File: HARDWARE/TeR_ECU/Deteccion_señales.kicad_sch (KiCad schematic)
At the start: 4 parts

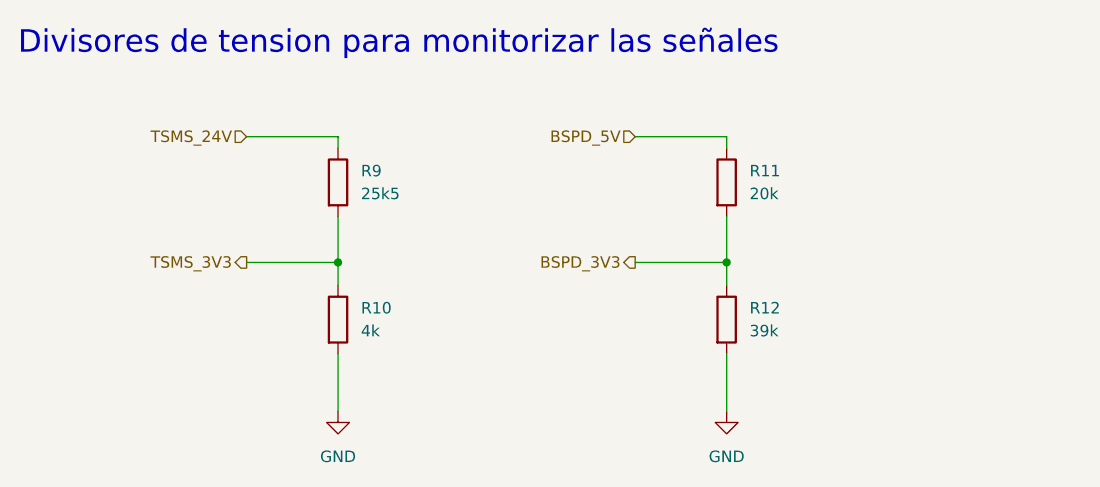
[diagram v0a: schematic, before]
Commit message: Rethought layout and footprints and fixed fuse normative problem
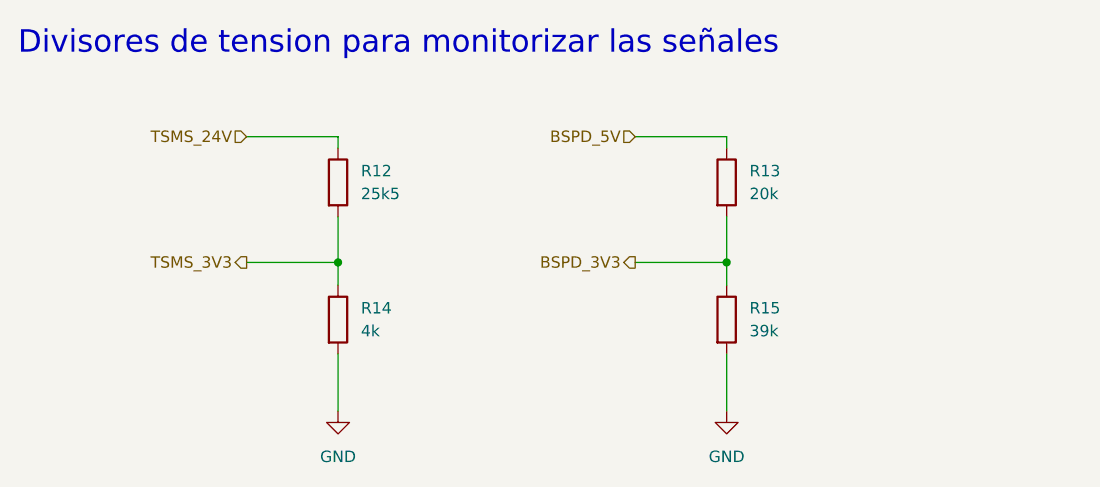
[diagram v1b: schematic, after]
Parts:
- renumbered R9 to R12, R11 to R13, R10 to R14, R12 to R15
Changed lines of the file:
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@@
   (symbol (lib_id "Device:R") (at 121.92 72.39 0) (unit 1)
     (in_bom yes) (on_board yes) (dnp no) (fields_autoplaced)
-    (property "Reference" "R9" (at 124.46 71.12 0)
+    (property "Reference" "R12" (at 124.46 71.12 0)
       (effects (font (size 1.27 1.27)) (justify left))
     )
@@
       (project "TeR_ECU"
         (path "/84413845-c4f3-4743-bcd2-a67649c90902/a7e5ef7e-c831-4d4f-a194-90a98bc5e16b"
-          (reference "R9") (unit 1)
+          (reference "R12") (unit 1)
         )
       )
@@
   (symbol (lib_id "Device:R") (at 165.1 87.63 0) (unit 1)
     (in_bom yes) (on_board yes) (dnp no) (fields_autoplaced)
-    (property "Reference" "R12" (at 167.64 86.36 0)
+    (property "Reference" "R15" (at 167.64 86.36 0)
       (effects (font (size 1.27 1.27)) (justify left))
     )
@@
       (project "TeR_ECU"
         (path "/84413845-c4f3-4743-bcd2-a67649c90902/a7e5ef7e-c831-4d4f-a194-90a98bc5e16b"
-          (reference "R12") (unit 1)
+          (reference "R15") (unit 1)
         )
       )
@@
   (symbol (lib_id "power:GND") (at 165.1 97.79 0) (unit 1)
     (in_bom yes) (on_board yes) (dnp no) (fields_autoplaced)
-    (property "Reference" "#PWR046" (at 165.1 104.14 0)
+    (property "Reference" "#PWR054" (at 165.1 104.14 0)
       (effects (font (size 1.27 1.27)) hide)
     )
@@
       (project "TeR_ECU"
         (path "/84413845-c4f3-4743-bcd2-a67649c90902/a7e5ef7e-c831-4d4f-a194-90a98bc5e16b"
-          (reference "#PWR046") (unit 1)
+          (reference "#PWR054") (unit 1)
         )
       )
@@
   (symbol (lib_id "power:GND") (at 121.92 97.79 0) (unit 1)
     (in_bom yes) (on_board yes) (dnp no) (fields_autoplaced)
-    (property "Reference" "#PWR044" (at 121.92 104.14 0)
+    (property "Reference" "#PWR053" (at 121.92 104.14 0)
       (effects (font (size 1.27 1.27)) hide)
     )
@@
       (project "TeR_ECU"
         (path "/84413845-c4f3-4743-bcd2-a67649c90902/a7e5ef7e-c831-4d4f-a194-90a98bc5e16b"
-          (reference "#PWR044") (unit 1)
+          (reference "#PWR053") (unit 1)
         )
       )
@@
   (symbol (lib_id "Device:R") (at 165.1 72.39 0) (unit 1)
     (in_bom yes) (on_board yes) (dnp no) (fields_autoplaced)
-    (property "Reference" "R11" (at 167.64 71.12 0)
+    (property "Reference" "R13" (at 167.64 71.12 0)
       (effects (font (size 1.27 1.27)) (justify left))
     )
@@
       (project "TeR_ECU"
         (path "/84413845-c4f3-4743-bcd2-a67649c90902/a7e5ef7e-c831-4d4f-a194-90a98bc5e16b"
-          (reference "R11") (unit 1)
+          (reference "R13") (unit 1)
         )
       )
@@
   (symbol (lib_id "Device:R") (at 121.92 87.63 0) (unit 1)
     (in_bom yes) (on_board yes) (dnp no) (fields_autoplaced)
-    (property "Reference" "R10" (at 124.46 86.36 0)
+    (property "Reference" "R14" (at 124.46 86.36 0)
       (effects (font (size 1.27 1.27)) (justify left))
     )
@@
       (project "TeR_ECU"
         (path "/84413845-c4f3-4743-bcd2-a67649c90902/a7e5ef7e-c831-4d4f-a194-90a98bc5e16b"
-          (reference "R10") (unit 1)
+          (reference "R14") (unit 1)
         )
       )

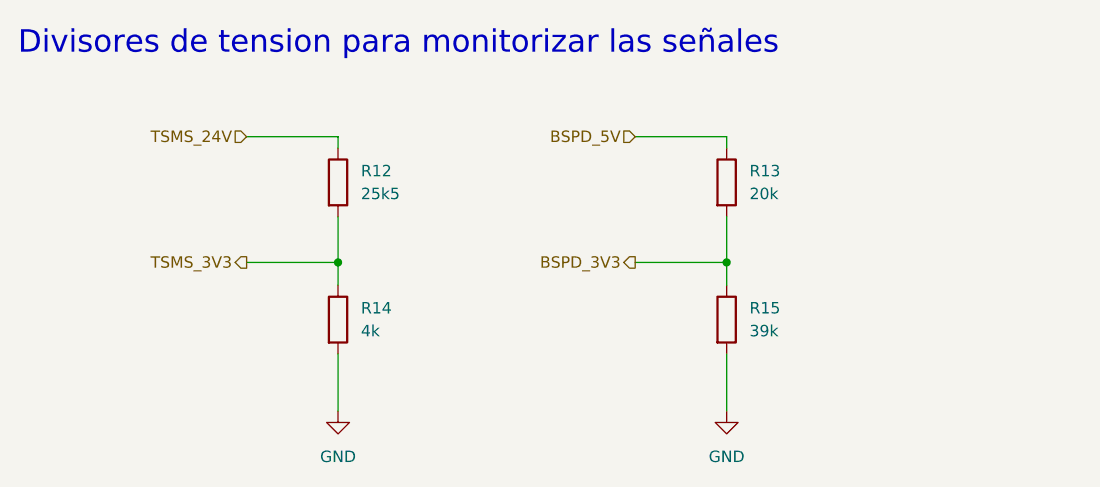
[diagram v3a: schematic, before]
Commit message: Advanced design and added IMU/GPS moduleç
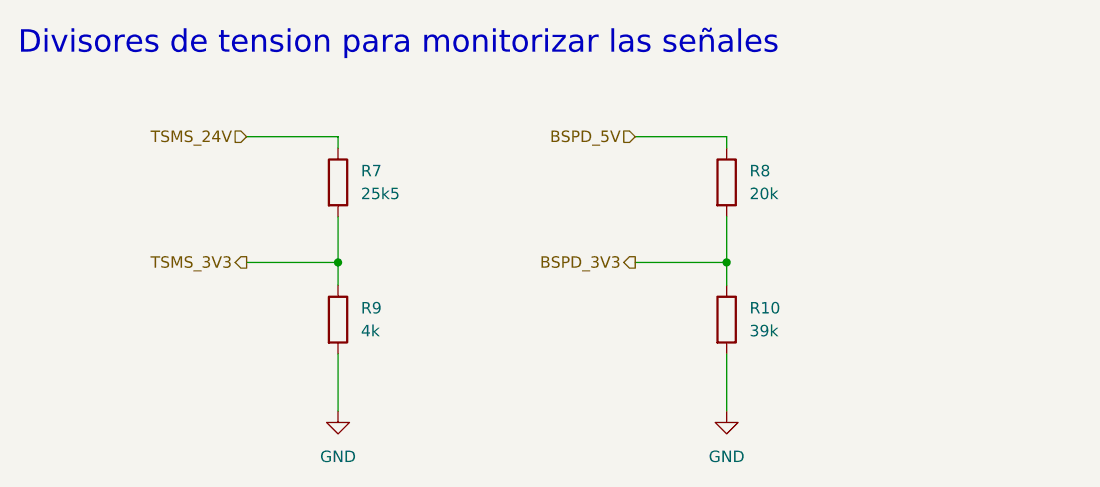
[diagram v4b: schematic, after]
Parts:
- renumbered R15 to R10, R12 to R7, R13 to R8, R14 to R9
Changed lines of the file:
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@@
 		(dnp no)
 		(fields_autoplaced yes)
-		(property "Reference" "R12"
+		(property "Reference" "R7"
 			(at 124.46 71.12 0)
 			(effects
@@
 			(project "TeR_ECU"
 				(path "/84413845-c4f3-4743-bcd2-a67649c90902/a7e5ef7e-c831-4d4f-a194-90a98bc5e16b"
-					(reference "R12")
+					(reference "R7")
 					(unit 1)
 				)
@@
 		(dnp no)
 		(fields_autoplaced yes)
-		(property "Reference" "R15"
+		(property "Reference" "R10"
 			(at 167.64 86.36 0)
 			(effects
@@
 			(project "TeR_ECU"
 				(path "/84413845-c4f3-4743-bcd2-a67649c90902/a7e5ef7e-c831-4d4f-a194-90a98bc5e16b"
-					(reference "R15")
+					(reference "R10")
 					(unit 1)
 				)
@@
 		(dnp no)
 		(fields_autoplaced yes)
-		(property "Reference" "#PWR054"
+		(property "Reference" "#PWR039"
 			(at 165.1 104.14 0)
 			(effects
@@
 			(project "TeR_ECU"
 				(path "/84413845-c4f3-4743-bcd2-a67649c90902/a7e5ef7e-c831-4d4f-a194-90a98bc5e16b"
-					(reference "#PWR054")
+					(reference "#PWR039")
 					(unit 1)
 				)
@@
 		(dnp no)
 		(fields_autoplaced yes)
-		(property "Reference" "#PWR053"
+		(property "Reference" "#PWR038"
 			(at 121.92 104.14 0)
 			(effects
@@
 			(project "TeR_ECU"
 				(path "/84413845-c4f3-4743-bcd2-a67649c90902/a7e5ef7e-c831-4d4f-a194-90a98bc5e16b"
-					(reference "#PWR053")
+					(reference "#PWR038")
 					(unit 1)
 				)
@@
 		(dnp no)
 		(fields_autoplaced yes)
-		(property "Reference" "R13"
+		(property "Reference" "R8"
 			(at 167.64 71.12 0)
 			(effects
@@
 			(project "TeR_ECU"
 				(path "/84413845-c4f3-4743-bcd2-a67649c90902/a7e5ef7e-c831-4d4f-a194-90a98bc5e16b"
-					(reference "R13")
+					(reference "R8")
 					(unit 1)
 				)
@@
 		(dnp no)
 		(fields_autoplaced yes)
-		(property "Reference" "R14"
+		(property "Reference" "R9"
 			(at 124.46 86.36 0)
 			(effects
@@
 			(project "TeR_ECU"
 				(path "/84413845-c4f3-4743-bcd2-a67649c90902/a7e5ef7e-c831-4d4f-a194-90a98bc5e16b"
-					(reference "R14")
-					(unit 1)
-				)
+					(reference "R9")
+					(unit 1)
+				)
